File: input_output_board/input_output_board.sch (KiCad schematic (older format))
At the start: 19 parts, among them J1 Neutrik_NCJ6FA-H-0, J2 Neutrik_NCJ6FA-H-0, J3 Neutrik_NCJ6FA-H-0, J4 Neutrik_NCJ6FA-H-0, J5 Neutrik_NCJ6FA-H-0, J6 Conn_02x05_Odd_Even, J7 Molex_SL_01x02_Male, J8 Molex_SL_01x02_Male, J9 Molex_SL_01x02_Male, K1 G6S-2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

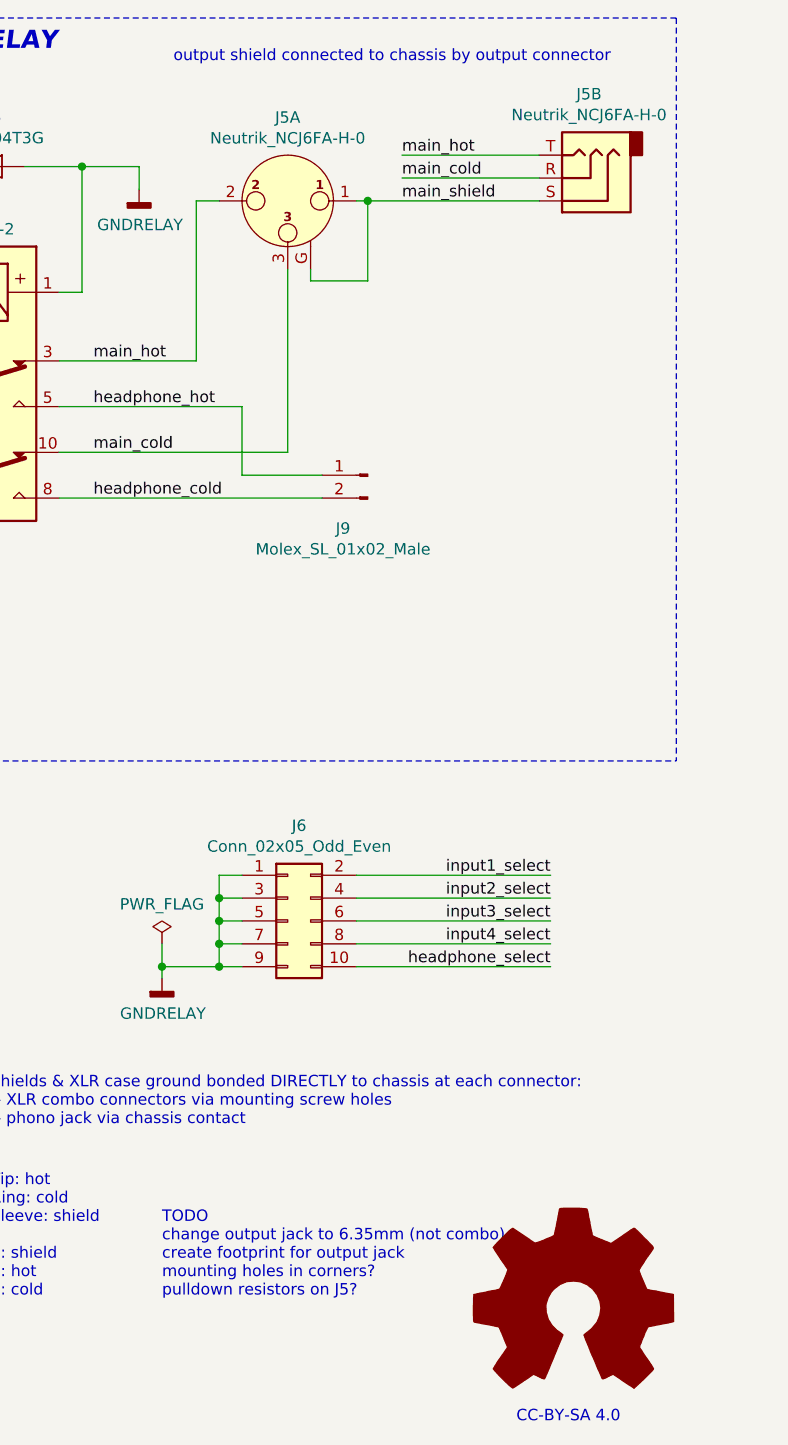
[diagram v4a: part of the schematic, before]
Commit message: move input/output connectors to line up with board edge, change output connector to XLR, adjust relay ground plane
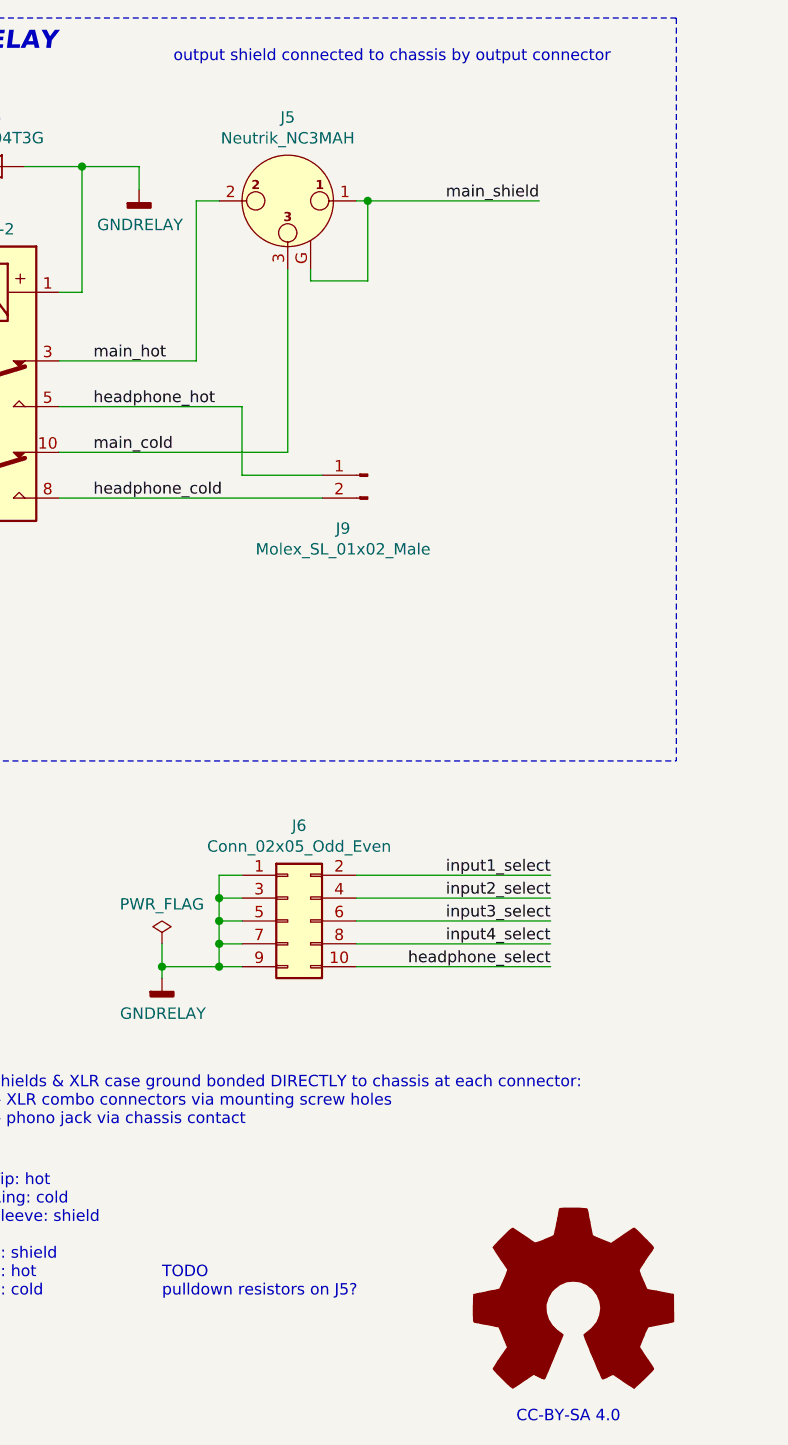
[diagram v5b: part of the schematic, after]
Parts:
- removed J5: Neutrik_NCJ6FA-H-0, Connector_Audio_project:Jack_XLR-6.35mm_Neutrik_NCJ6FA-H-0_Horizontal, symbol Connector_gkeeth:Neutrik_NCJ6FA-H-0
- added J5: Neutrik_NC3MAH, Connector_Audio_project:Jack_XLR_Neutrik_NC3MAH_Horizontal, symbol Connector_gkeeth:Neutrik_NC3MAH
- J1, J2, J3, J4: Distributor PN 568-NCJ6FA-H -> 568-NCJ6FA-H-0; Manufacturer PN NCJ6FA-H -> NCJ6FA-H-0; URL https://www.mouser.com/ProductDetail/Neutrik/NCJ6FA-H?qs=aE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 -> https://www.mouser.com/ProductDetail/Neutrik/NCJ6FA-H-0?qs=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; Unit Price 2.10 -> 2.14
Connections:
- net main_cold: now also J5.3
- net main_hot: now also J5.2
- net main_shield: now also J5.1, J5.G
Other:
- note added: "TODO\npulldown resistors on J5?"
- note removed: "TODO\nchange output jack to 6.35mm (not combo)\ncreate footprint for output jack\nmounting holes in corners?\npulldown resistors on J5?"

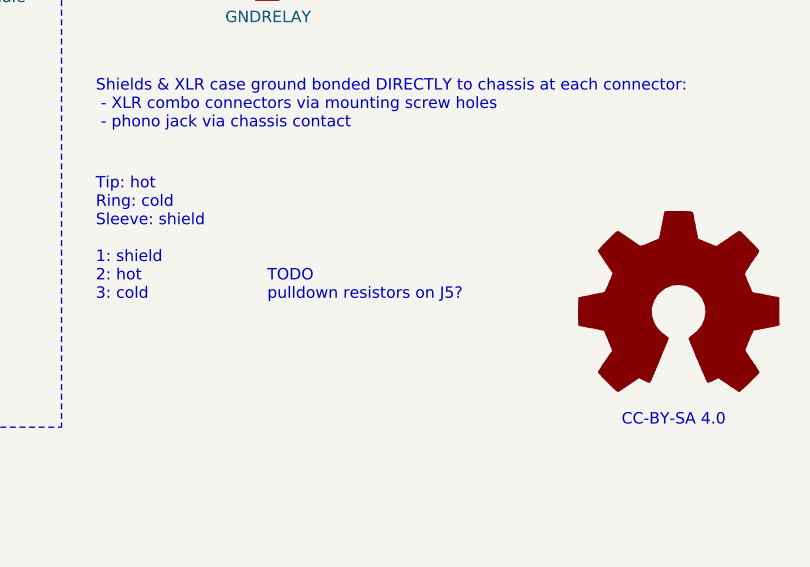
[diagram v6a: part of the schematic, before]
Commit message: remove TODO from input/output schematic -- not adding pulldown resistors to main output
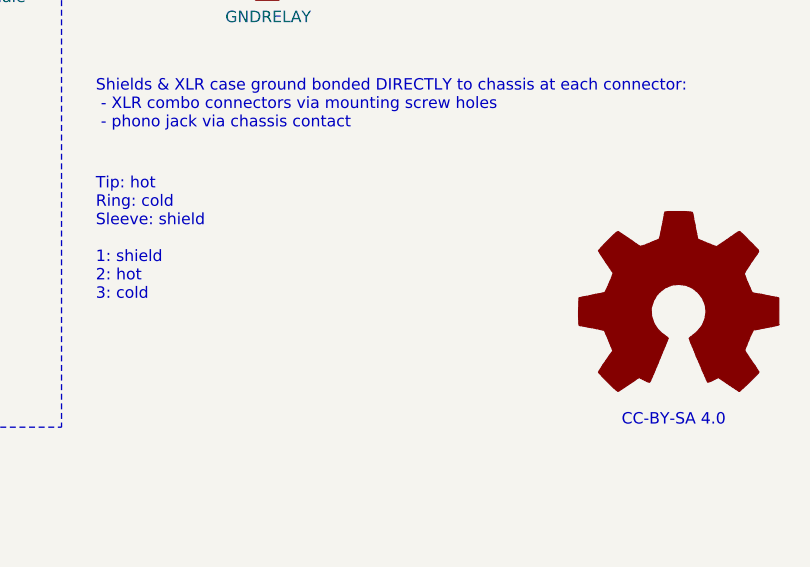
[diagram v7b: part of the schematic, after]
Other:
- note removed: "TODO\npulldown resistors on J5?"
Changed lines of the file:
@@
 Text Notes 800  7550 0    50   ~ 0
 input shield connected to chassis by input connector
-Text Notes 8200 6150 0    50   ~ 0
-TODO\npulldown resistors on J5?
 $Comp
 L power_gkeeth:GNDRELAY #PWR0102

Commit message: fill out all input/output board BOM info
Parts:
- J6: Distributor (none) -> Digikey; Distributor PN (none) -> WM9219-ND; Manufacturer (none) -> Molex; Manufacturer PN (none) -> 0702461001; URL (none) -> https://www.digikey.com/products/en?keywords=70246-1001; Unit Price (none) -> 1.70
- J7, J9: Distributor PN (none) -> WM4900-ND; Manufacturer PN 0705430003 -> 0705430001; URL (none) -> https://www.digikey.com/products/en?keywords=70553-0001; Unit Price (none) -> 0.74
- J8: Distributor PN (none) -> WM4900-ND; URL (none) -> https://www.digikey.com/products/en?keywords=70553-0001; Unit Price (none) -> 0.74
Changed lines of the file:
@@
 F 3 "https://www.molex.com/pdm_docs/sd/705430001_sd.pdf" H 6350 4700 50  0001 C CNN
 F 4 "Molex" H 6350 4700 50  0001 C CNN "Manufacturer"
-F 5 "0705430003" H 6350 4700 50  0001 C CNN "Manufacturer PN"
+F 5 "0705430001" H 6350 4700 50  0001 C CNN "Manufacturer PN"
 F 6 "Digikey" H 6350 4700 50  0001 C CNN "Distributor"
+F 7 "WM4900-ND" H 6350 4700 50  0001 C CNN "Distributor PN"
+F 8 "https://www.digikey.com/products/en?keywords=70553-0001" H 6350 4700 50  0001 C CNN "URL"
+F 9 "0.74" H 6350 4700 50  0001 C CNN "Unit Price"
 	1    6350 4700
 	-1   0    0    -1
@@
 F 1 "Conn_02x05_Odd_Even" H 8800 4826 50  0000 C CNN
 F 2 "Connector_Molex_C-Grid:Molex_C-Grid_70246-1001_2x05_P2.54mm_Vertical" H 8750 4500 50  0001 C CNN
-F 3 "~" H 8750 4500 50  0001 C CNN
+F 3 "https://www.molex.com/pdm_docs/sd/702461001_sd.pdf" H 8750 4500 50  0001 C CNN
+F 4 "Digikey" H 8750 4500 50  0001 C CNN "Distributor"
+F 5 "WM9219-ND" H 8750 4500 50  0001 C CNN "Distributor PN"
+F 6 "Molex" H 8750 4500 50  0001 C CNN "Manufacturer"
+F 7 "0702461001" H 8750 4500 50  0001 C CNN "Manufacturer PN"
+F 8 "https://www.digikey.com/products/en?keywords=70246-1001" H 8750 4500 50  0001 C CNN "URL"
+F 9 "1.70" H 8750 4500 50  0001 C CNN "Unit Price"
 	1    8750 4500
 	1    0    0    -1
@@
 F 5 "0705430001" H 6300 2150 50  0001 C CNN "Manufacturer PN"
 F 6 "Digikey" H 6300 2150 50  0001 C CNN "Distributor"
+F 7 "WM4900-ND" H 6300 2150 50  0001 C CNN "Distributor PN"
+F 8 "https://www.digikey.com/products/en?keywords=70553-0001" H 6300 2150 50  0001 C CNN "URL"
+F 9 "0.74" H 6300 2150 50  0001 C CNN "Unit Price"
 	1    6300 2150
 	1    0    0    -1
@@
 F 3 "https://www.molex.com/pdm_docs/sd/705430001_sd.pdf" H 9100 2550 50  0001 C CNN
 F 4 "Molex" H 9100 2550 50  0001 C CNN "Manufacturer"
-F 5 "0705430003" H 9100 2550 50  0001 C CNN "Manufacturer PN"
+F 5 "0705430001" H 9100 2550 50  0001 C CNN "Manufacturer PN"
 F 6 "Digikey" H 9100 2550 50  0001 C CNN "Distributor"
+F 7 "WM4900-ND" H 9100 2550 50  0001 C CNN "Distributor PN"
+F 8 "https://www.digikey.com/products/en?keywords=70553-0001" H 9100 2550 50  0001 C CNN "URL"
+F 9 "0.74" H 9100 2550 50  0001 C CNN "Unit Price"
 	1    9100 2550
 	-1   0    0    -1
